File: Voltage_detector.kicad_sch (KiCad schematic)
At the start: 11 parts, among them Q4 Q_NMOS_GSD, U6 LM393

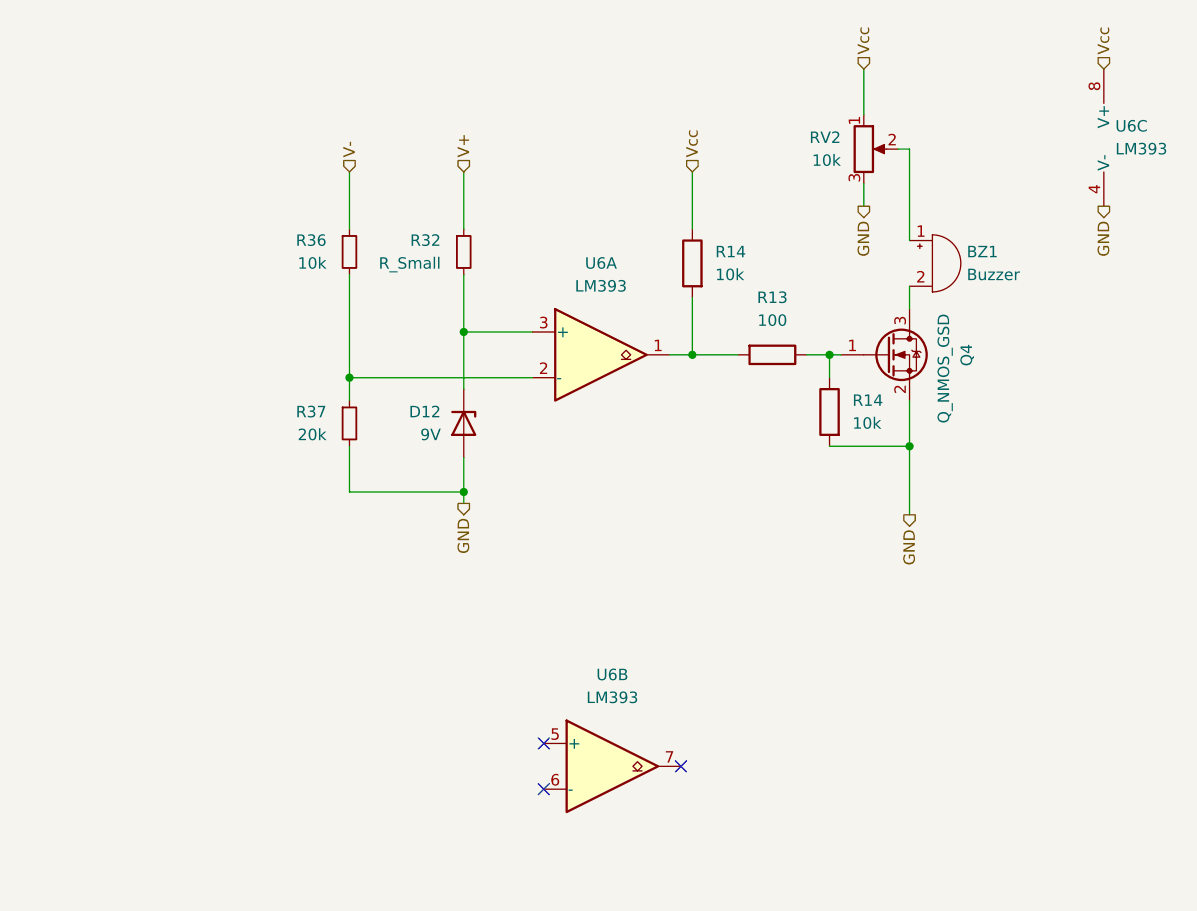
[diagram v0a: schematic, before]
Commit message: update art work
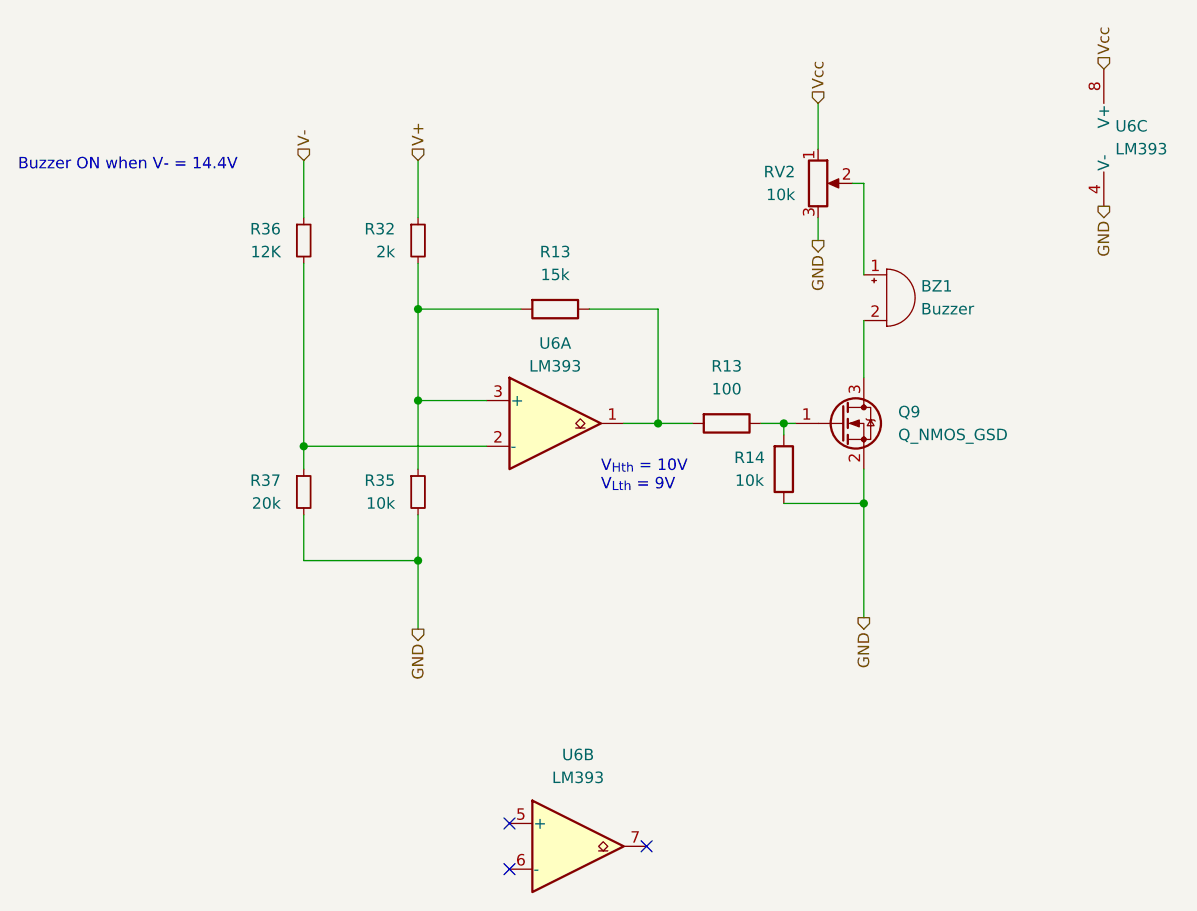
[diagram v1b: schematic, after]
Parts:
- removed D12: 9V, symbol Device:D_Zener
- removed Q4: Q_NMOS_GSD, Package_TO_SOT_SMD:SOT-23, symbol Device:Q_NMOS_GSD
- removed R14 (x2): 10k, Resistor_SMD:R_0402_1005Metric, symbol Device:R
- added Q9: Q_NMOS_GSD, Package_TO_SOT_SMD:SOT-23, symbol Device:Q_NMOS_GSD
- added R13: 15k, Resistor_SMD:R_0402_1005Metric, symbol Device:R
- added R14: 10k, Resistor_SMD:R_0402_1005Metric, symbol Device:R
- added R35: 10k, Resistor_SMD:R_0402_1005Metric, symbol Device:R_Small
- R32: value R_Small -> 2k
- R36: value 10k -> 12K
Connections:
- net GND: now also Q9.2 (S), R14.1, R35.2
- net at R13.2, U6.1: now also R13.1
- net at R32.2, U6.3 (+): now also R13.2, R35.1
- net at R13.1: now also Q9.1 (G), R14.2
- net at BZ1.2 (+): now also Q9.3 (D)
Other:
- note added: "Buzzer ON when V- = 14.4V"
- note added: "V_{Hth} = 10V V_{Lth} = 9V"
- moved on the sheet: R13, R32, R36, R37, RV2, U6A, U6B

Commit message: アートワークのほとんど終わり
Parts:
- Q9: LCSC (none) -> C7420346
- R13: LCSC (none) -> C25076
- R13: LCSC (none) -> C25756
- R14, R35: LCSC (none) -> C25744
- R32: value 2k -> 2.4k; LCSC (none) -> C25882
- R36: value 12K -> 12k; LCSC (none) -> C25752
- R37: LCSC (none) -> C25765
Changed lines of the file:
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@@
       (effects (font (size 1.27 1.27)) (justify right))
     )
-    (property "Value" "2k" (at 77.47 40.64 0)
+    (property "Value" "2.4k" (at 77.47 40.64 0)
       (effects (font (size 1.27 1.27)) (justify right))
     )
@@
     )
     (property "Datasheet" "~" (at 80.01 39.37 0)
+      (effects (font (size 1.27 1.27)) hide)
+    )
+    (property "LCSC" "C25882" (at 80.01 39.37 0)
       (effects (font (size 1.27 1.27)) hide)
     )
@@
       (effects (font (size 1.27 1.27)) hide)
     )
+    (property "LCSC" "C25076" (at 114.3 59.69 0)
+      (effects (font (size 1.27 1.27)) hide)
+    )
     (pin "2")
     (pin "1")
@@
       (effects (font (size 1.27 1.27)) hide)
     )
+    (property "LCSC" "C7420346" (at 127 59.69 0)
+      (effects (font (size 1.27 1.27)) hide)
+    )
     (pin "2")
     (pin "3")
@@
       (effects (font (size 1.27 1.27)) hide)
     )
+    (property "LCSC" "C25765" (at 67.31 67.31 0)
+      (effects (font (size 1.27 1.27)) hide)
+    )
     (pin "1")
     (pin "2")
@@
       (effects (font (size 1.27 1.27)) (justify right))
     )
-    (property "Value" "12K" (at 64.77 40.64 0)
+    (property "Value" "12k" (at 64.77 40.64 0)
       (effects (font (size 1.27 1.27)) (justify right))
     )
@@
       (effects (font (size 1.27 1.27)) hide)
     )
+    (property "LCSC" "C25752" (at 67.31 39.37 0)
+      (effects (font (size 1.27 1.27)) hide)
+    )
     (pin "1")
     (pin "2")
@@
     )
     (property "name" "" (at 95.25 46.99 0)
+      (effects (font (size 1.27 1.27)) hide)
+    )
+    (property "LCSC" "C25756" (at 95.25 46.99 0)
       (effects (font (size 1.27 1.27)) hide)
     )
@@
       (effects (font (size 1.27 1.27)) hide)
     )
+    (property "LCSC" "C25744" (at 120.65 64.77 0)
+      (effects (font (size 1.27 1.27)) hide)
+    )
     (pin "1")
     (pin "2")
@@
       (effects (font (size 1.27 1.27)) hide)
     )
+    (property "LCSC" "C25744" (at 80.01 67.31 0)
+      (effects (font (size 1.27 1.27)) hide)
+    )
